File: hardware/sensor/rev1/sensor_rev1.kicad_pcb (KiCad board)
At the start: 2 copper layers, 68.9 x 28.9 mm, 52 parts, among them IC1 STM8L051F3P6, IC2 CC1101RGPR, J1 22-28-4044, J2 M20-9770342, Y1 NX3225GA-26.000M-STD-CRG-2

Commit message: EG-49 Takachi PCB format.
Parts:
- removed LED3: TLHR4400-AS12Z, MyParts:TLHR4400AS12Z
- added LED1: APTD1608LSURCK, MyParts:LEDM168X95N, F.Cu at (204.2, 103.9)
- S1, S3: value MASM-14R-8-10 -> GP560_20-25; footprint MyParts:MASM14R810 -> MyParts:GP5602025; moved to F.Cu
- S2: value TL6120DF160QG -> PTS636SMG25JSMTR_LFS; footprint MyParts:TL6120DF160QG -> MyParts:PTS636SMG25JSMTRLFS
- moved C6 74.1 mm to (194.0, 99.6)
- moved C7 59.1 mm to (212.7, 100.9)
- moved C125 57.1 mm to (201.3, 108.3), turned to 90 degrees
- moved J1 57.1 mm to (216.3, 106.9), turned to 90 degrees
- moved L124 54.3 mm to (201.3, 110.3), turned to 90 degrees
- moved C123 52.0 mm to (201.8, 111.9), turned to 180 degrees
- moved L123 49.9 mm to (201.2, 113.4), turned to 90 degrees
- moved L132 47.4 mm to (200.3, 115.4), turned to 90 degrees
- moved C122 46.9 mm to (202.2, 115.5), turned to 90 degrees
- moved C124 45.2 mm to (203.9, 116.5), turned to -90 degrees
- moved C131 45.1 mm to (200.3, 117.0), turned to 180 degrees
- moved L122 44.7 mm to (202.3, 117.0), turned to 0 degrees
- moved C121 43.4 mm to (201.3, 118.1), turned to 180 degrees
- moved C14 41.6 mm to (198.6, 119.9), turned to 90 degrees
- moved C16 41.3 mm to (199.7, 119.9), turned to 90 degrees
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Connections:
- S2 pad 1: GND -> BTN
- S2 pad 3: BTN -> unconnected-(S2-GND_1-Pad3)
- S2 pad 4: BTN -> unconnected-(S2-GND_2-Pad4)
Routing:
- net VDD: track 15.2 -> 11.5 mm
- net Net-(LED1-A): track 3.01 -> 0.00 mm
- net GND: track 34.3 -> 32.8 mm, vias 80 -> 79
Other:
- board size 68.9 x 28.9 mm -> 28.9 x 68.9 mm
- board text added: "Exit Guardian Sensor REV1.0 NPX4U 2026"
- board text removed: "Exit Guardian - Sensor REV1.0 NPX4U 2026"

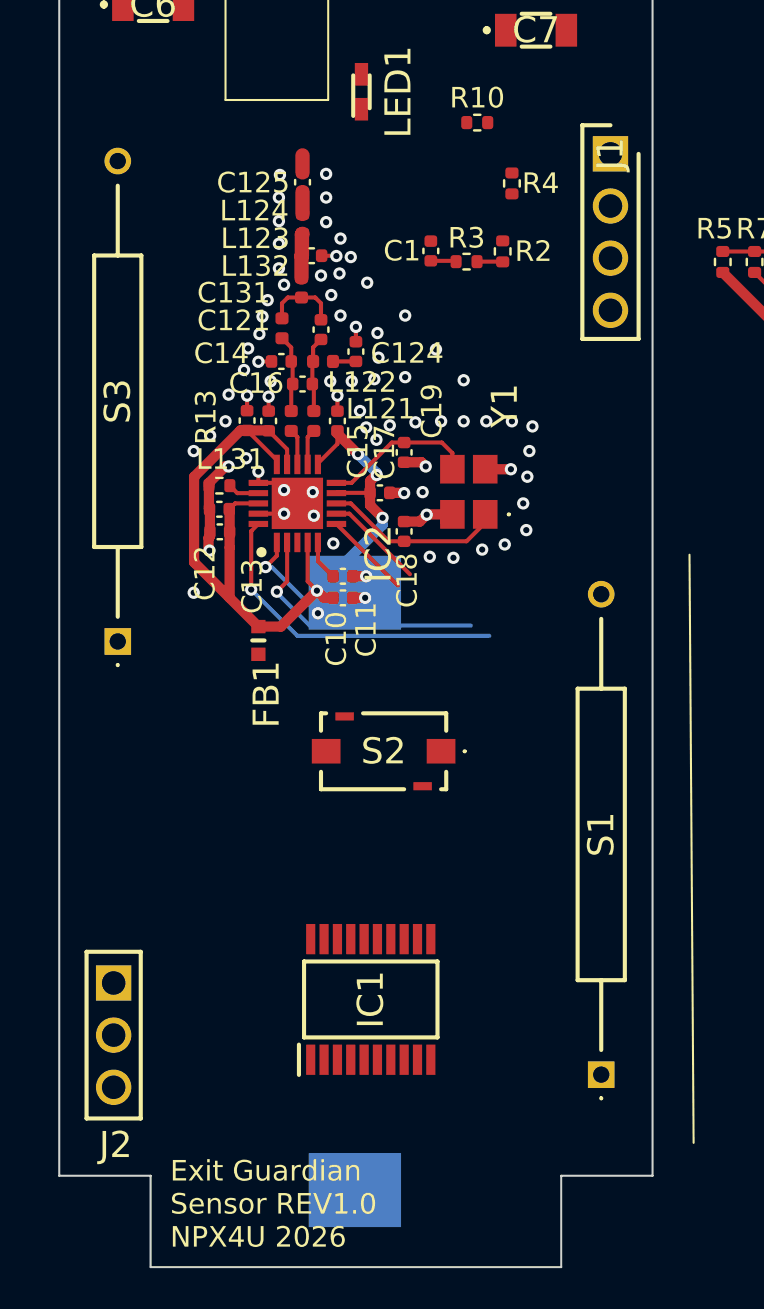
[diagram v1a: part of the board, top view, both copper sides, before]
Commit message: EG-49 CST2032 concluded and placed.
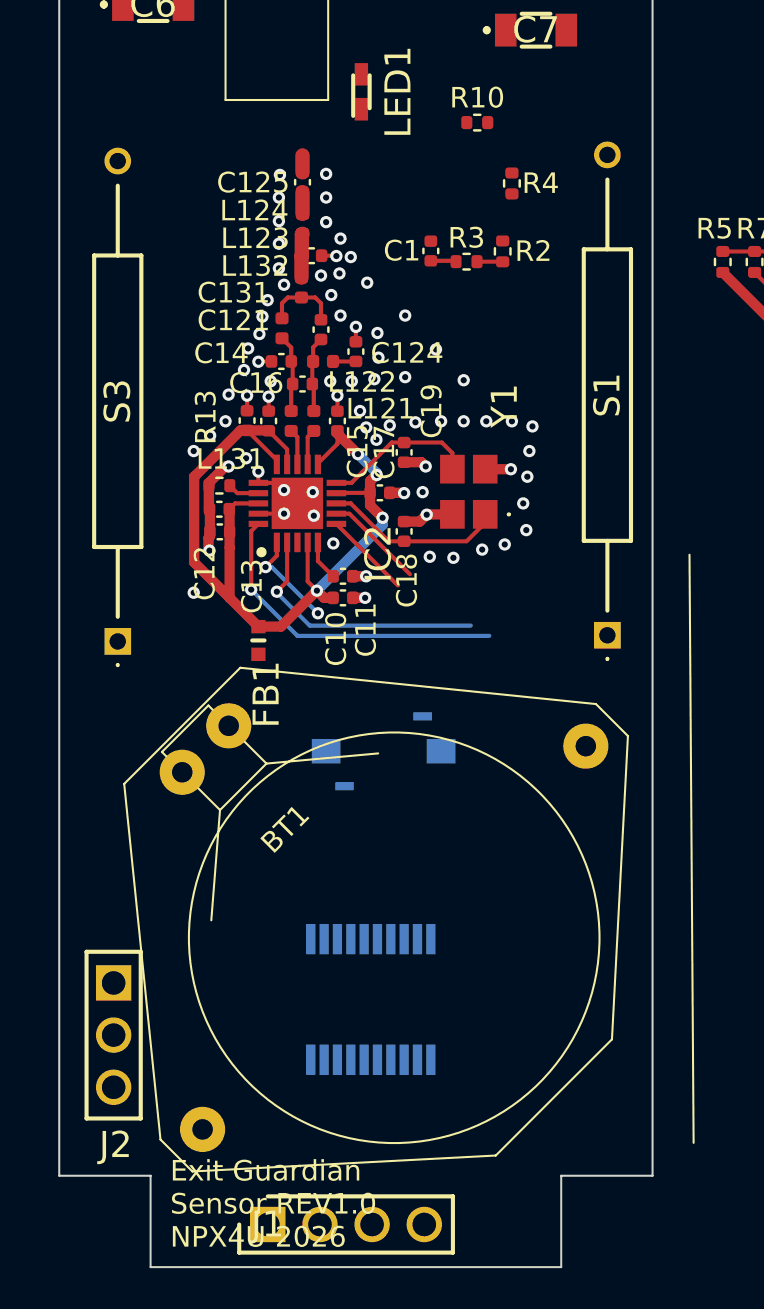
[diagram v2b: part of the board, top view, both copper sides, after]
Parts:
- BT1: value BAT-HLD-013-SMT-TR -> CST2032; footprint MyParts:BATHLD013SMTTR -> MyParts:CST2032; moved to F.Cu
- IC1, S2: moved to B.Cu
- moved J1 54.8 mm to (199.6, 159.1), turned to 180 degrees
- moved S1 21.4 mm to (216.2, 130.3)
- moved BT1 2.96 mm to (205.8, 145.1), turned to 45 degrees
- turned S2 to 0 degrees
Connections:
- BT1 pad 1: VDD -> GND

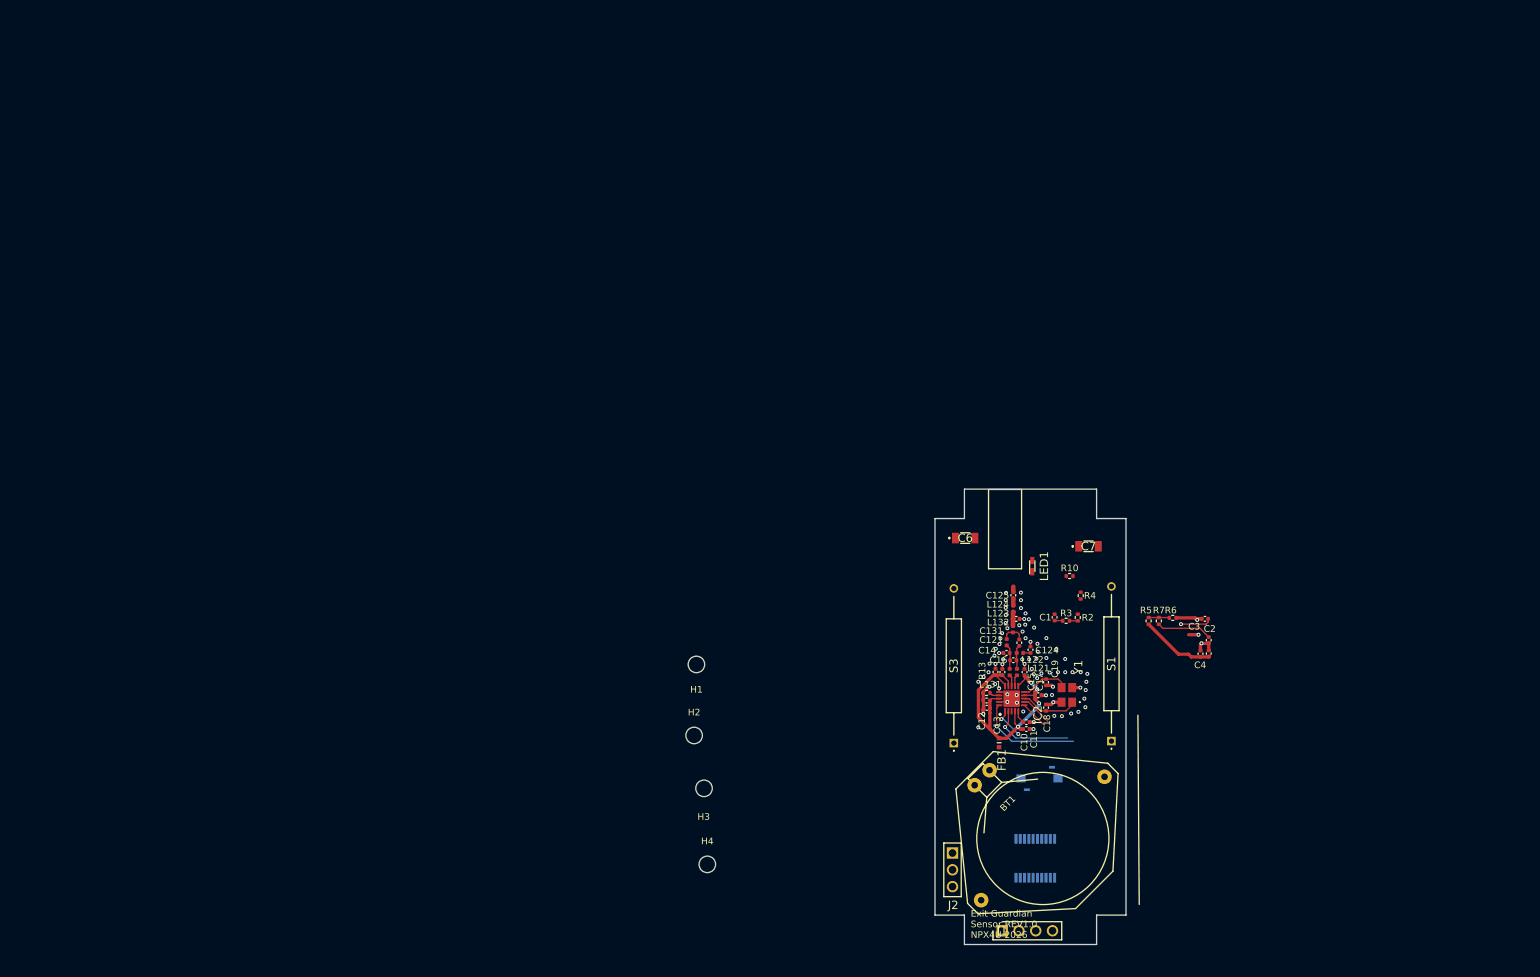
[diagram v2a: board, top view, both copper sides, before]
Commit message: EG-49 Board size and mounting holes placed.
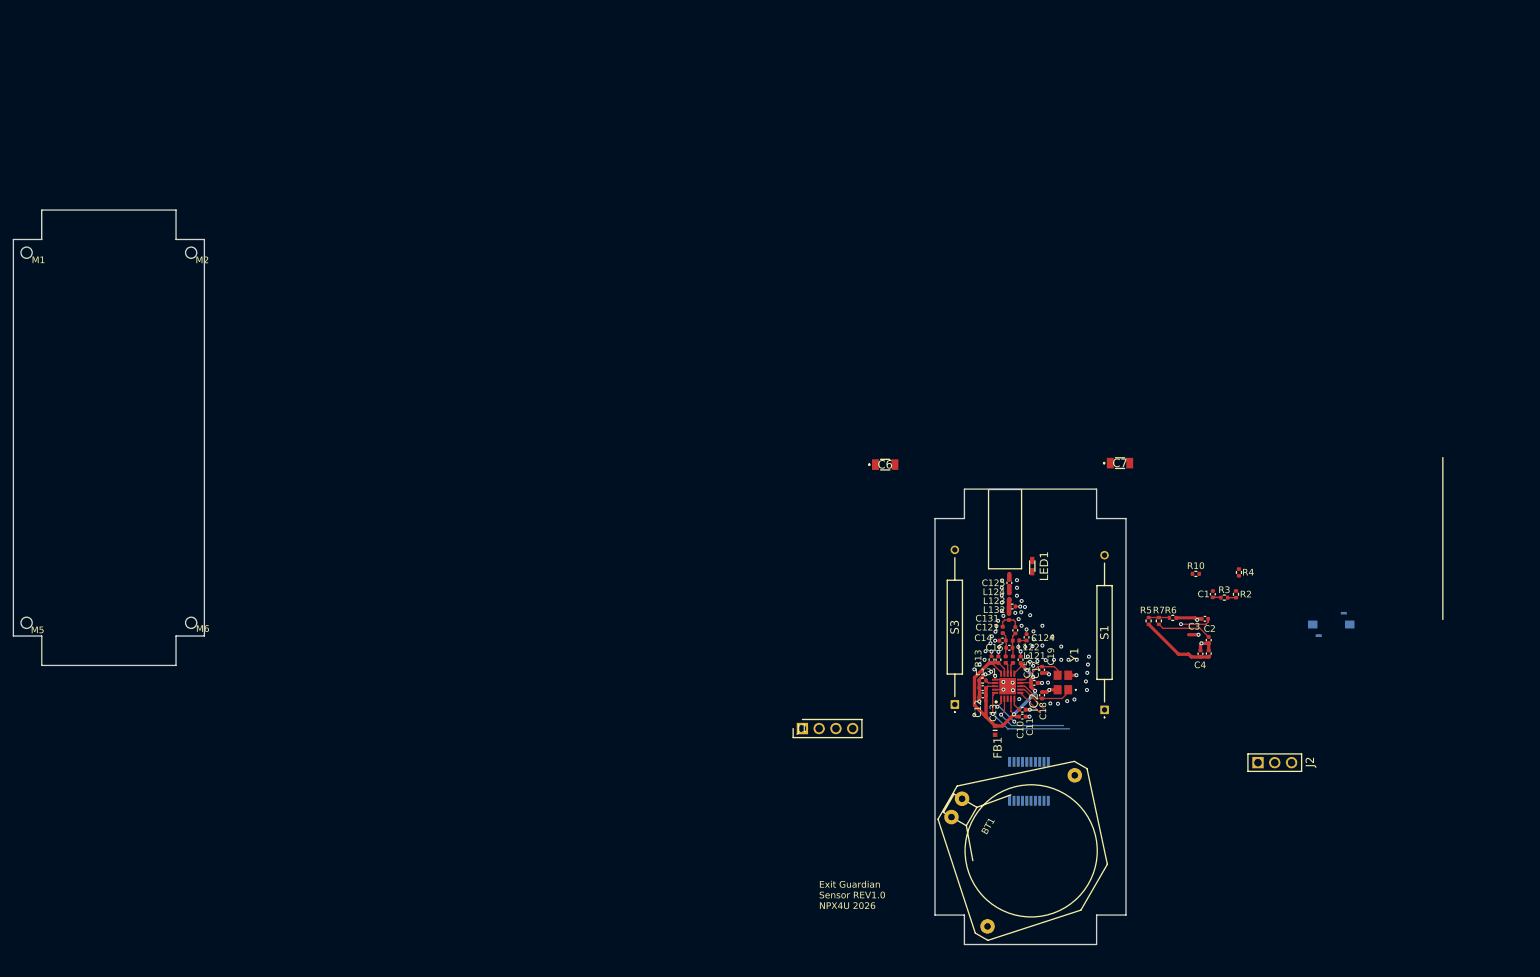
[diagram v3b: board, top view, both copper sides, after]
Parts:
- removed H1, H2, H3, H4: MountingHole, MountingHole:MountingHole_2.5mm
- added M1: ~, MyParts:MountingHole_1.7mm, F.Cu at (52.0, 56.5)
- added M2: ~, MyParts:MountingHole_1.7mm, F.Cu at (76.9, 56.5)
- added M5: ~, MyParts:MountingHole_1.7mm, F.Cu at (52.0, 112.5)
- added M6: ~, MyParts:MountingHole_1.7mm, F.Cu at (76.9, 112.5)
- moved S2 49.9 mm to (249.4, 112.7)
- moved J2 48.2 mm to (238.3, 133.6), turned to 0 degrees
- moved J1 43.0 mm to (169.4, 128.4)
- moved R2 24.2 mm to (235.0, 108.1)
- moved R3 24.2 mm to (233.2, 108.6)
- moved R4 24.2 mm to (235.4, 104.8)
- moved C1 24.2 mm to (231.5, 108.1)
- moved R10 19.1 mm to (228.9, 105.0)
- moved C6 16.4 mm to (181.9, 88.5)
- moved C7 13.5 mm to (217.4, 88.3)
- moved IC1 11.7 mm to (203.7, 136.4)
- moved S3 5.84 mm to (192.4, 124.8)
- moved S1 4.85 mm to (215.1, 125.6)
- moved BT1 2.58 mm to (204.0, 147.0), turned to 60 degrees
- moved C10 1.97 mm to (202.7, 126.7)
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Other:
- board size 28.9 x 68.9 mm -> 168.3 x 111.1 mm

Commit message: EG-49 Board placed.
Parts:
- moved M1 173.7 mm to (222.0, 92.0)
- moved M2 173.7 mm to (246.9, 92.0)
- moved M5 173.7 mm to (222.0, 148.0)
- moved M6 173.7 mm to (246.9, 148.0)
- moved J2 71.7 mm to (264.4, 66.8)
- moved C1 71.7 mm to (257.6, 41.4)
- moved C10 71.7 mm to (228.8, 59.9)
- moved C11 71.7 mm to (228.8, 58.8)
- moved C12 71.7 mm to (222.7, 55.6)
- moved C121 71.7 mm to (226.8, 49.5)
- moved C122 71.7 mm to (227.7, 46.8)
- moved C123 71.7 mm to (227.2, 43.2)
- moved C125 71.7 mm to (226.8, 39.6)
- moved C13 71.7 mm to (222.8, 56.7)
- moved C131 71.7 mm to (225.8, 48.4)
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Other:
- board size 168.3 x 111.1 mm -> 28.9 x 68.9 mm

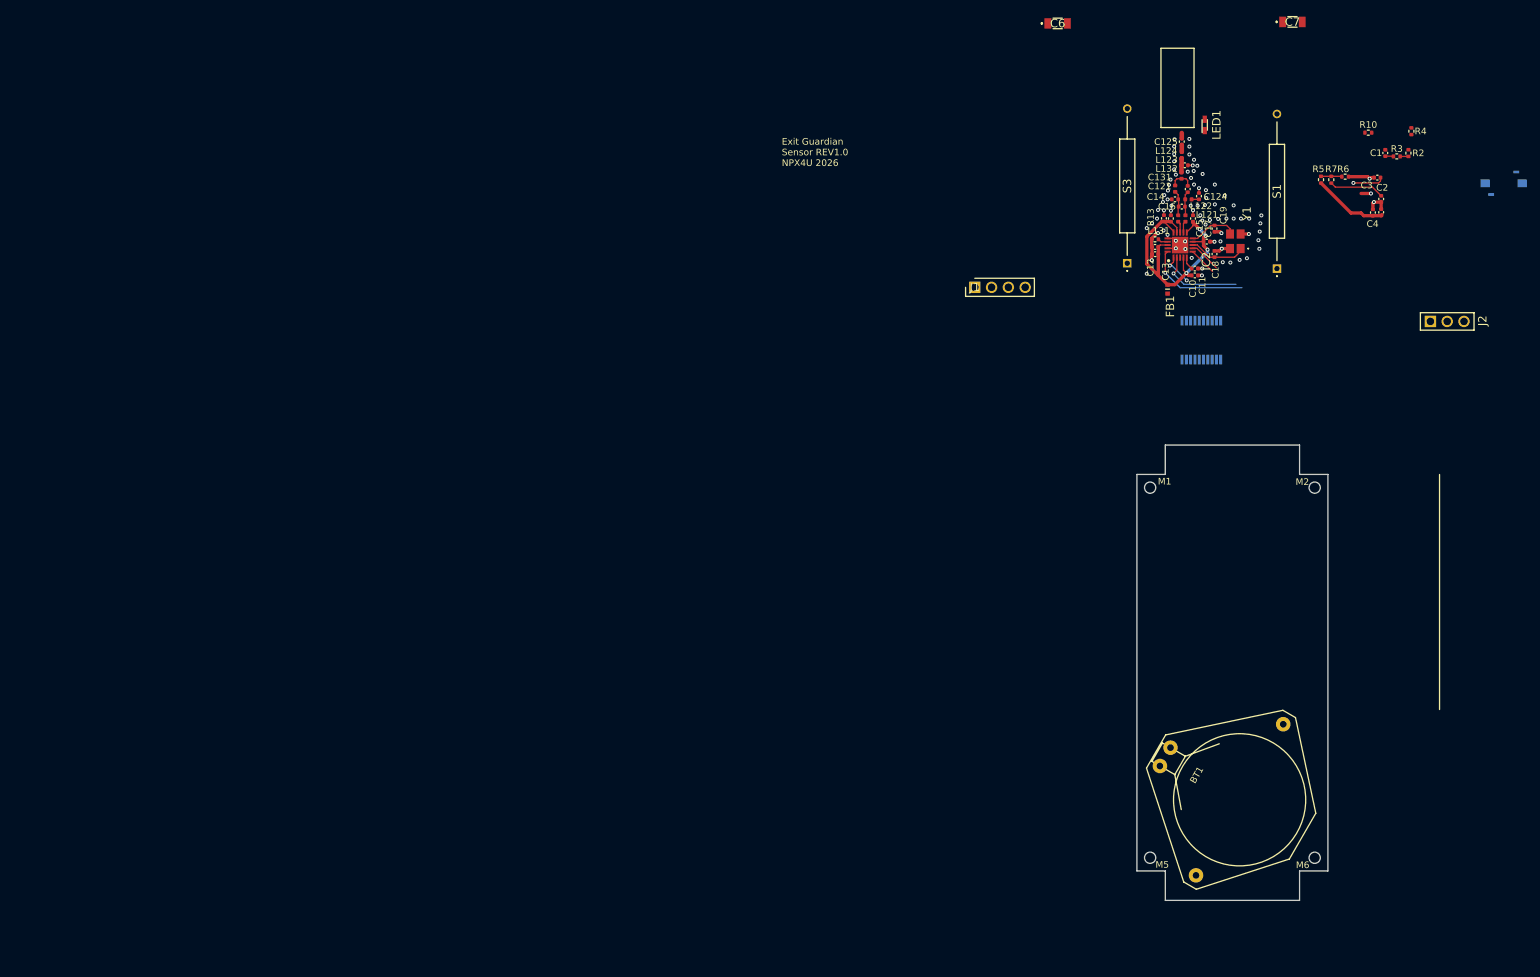
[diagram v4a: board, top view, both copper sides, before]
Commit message: EG-49 Battery holder on the right place.
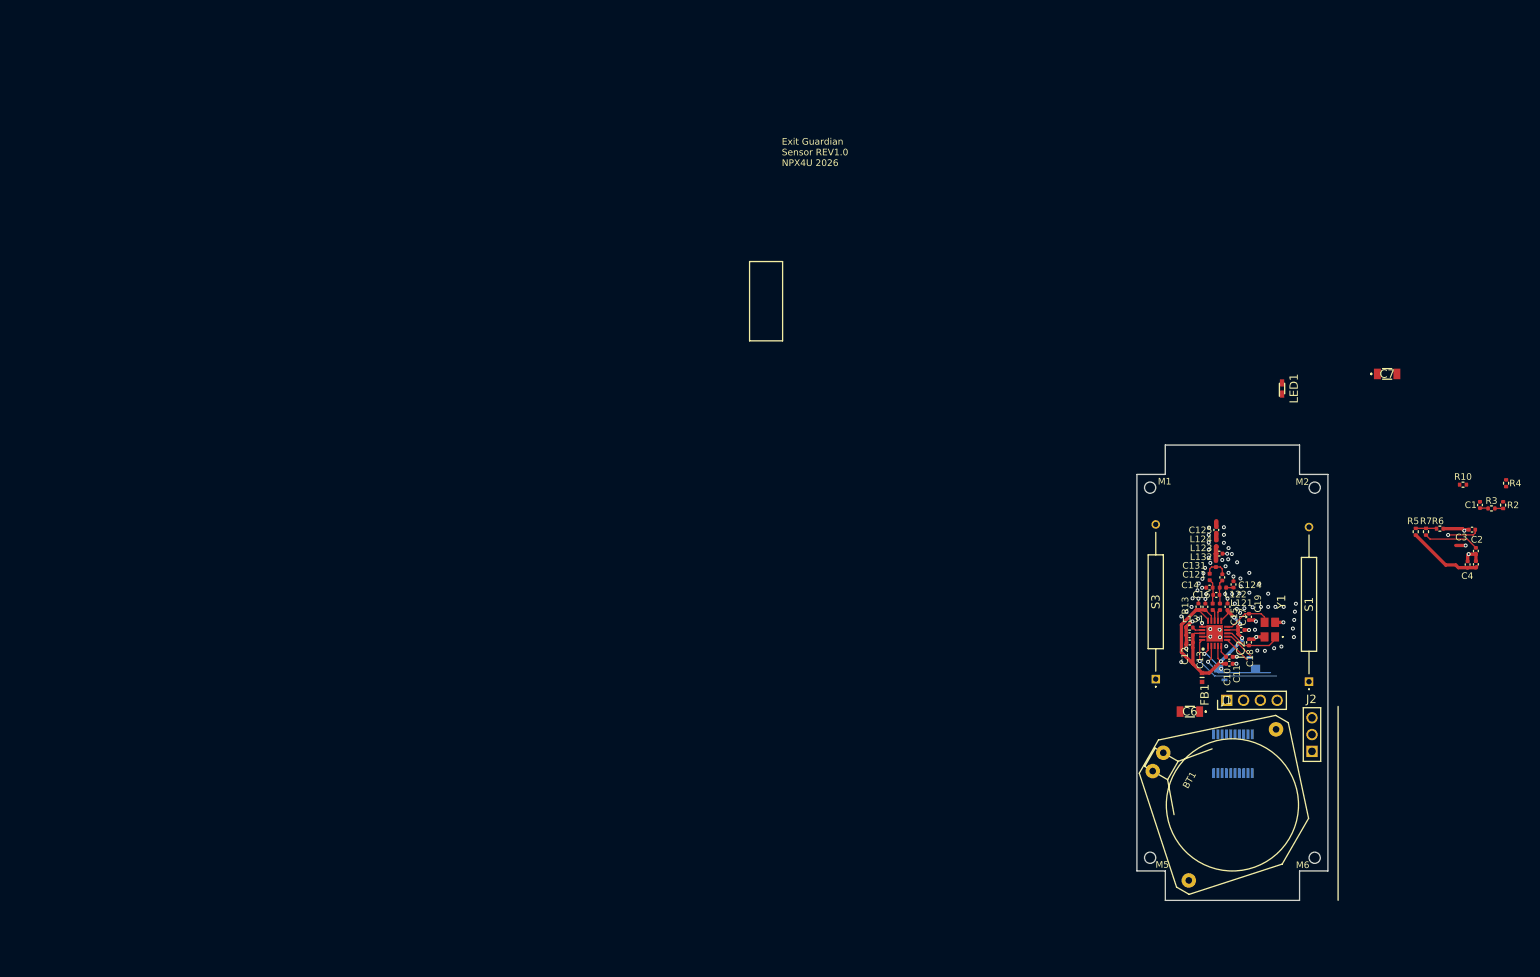
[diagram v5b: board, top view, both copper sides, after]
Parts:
- moved C6 106.0 mm to (228.0, 125.9), turned to 180 degrees
- moved S2 83.8 mm to (235.2, 119.4)
- moved J1 73.2 mm to (233.6, 124.2)
- moved J2 67.5 mm to (246.5, 131.9), turned to 90 degrees
- moved S3 63.1 mm to (222.8, 121.0)
- moved IC1 62.8 mm to (234.5, 132.3)
- moved S1 62.7 mm to (246.0, 121.4)
- moved C13 59.0 mm to (228.0, 115.4)
- moved L124 59.0 mm to (232.0, 100.4)
- moved R13 59.0 mm to (228.0, 113.2)
- moved C121 59.0 mm to (232.0, 108.2)
- moved C123 59.0 mm to (232.5, 102.0)
- moved C124 59.0 mm to (234.6, 106.7)
- moved C125 59.0 mm to (232.0, 98.4)
- moved C14 59.0 mm to (229.3, 110.0)
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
